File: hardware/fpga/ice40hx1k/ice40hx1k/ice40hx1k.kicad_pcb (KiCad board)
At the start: 2 copper layers, 96.8 x 77 mm, 58 parts, among them J1 Conn_01x20_Male, J2 Conn_01x20_Male, J3 Conn_01x20_Male, U1 LTC3406ES5, U5 AT25SF081-SSHD-X, U6 ICE40HX1K-VQ100(VQFP100), U7 AS7C34096A, X2 ASE-10MHz, X3 ASE-10MHz, X4 ASE-10MHz, X5 ASV-xxxMHz, X6 ASV-xxxMHz, X7 ASV-xxxMHz

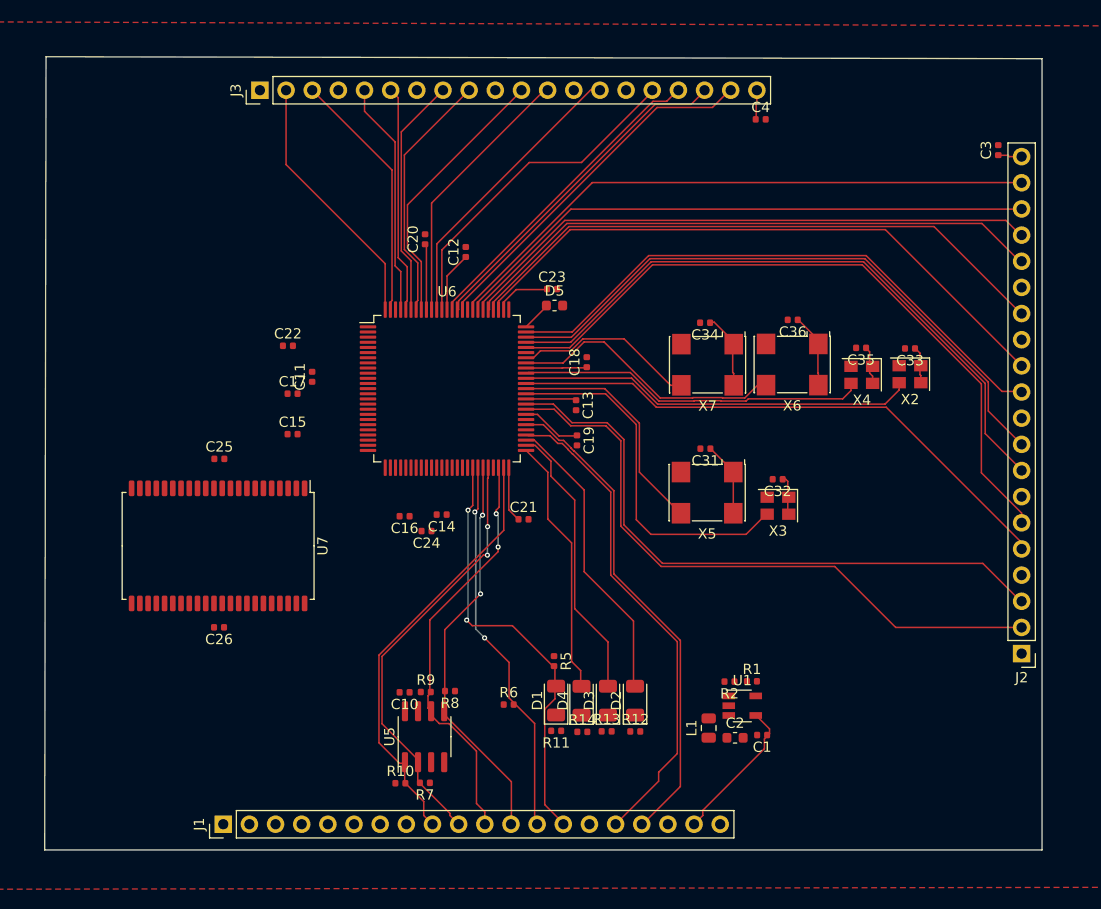
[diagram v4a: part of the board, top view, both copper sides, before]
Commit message: std FPGA skeleton
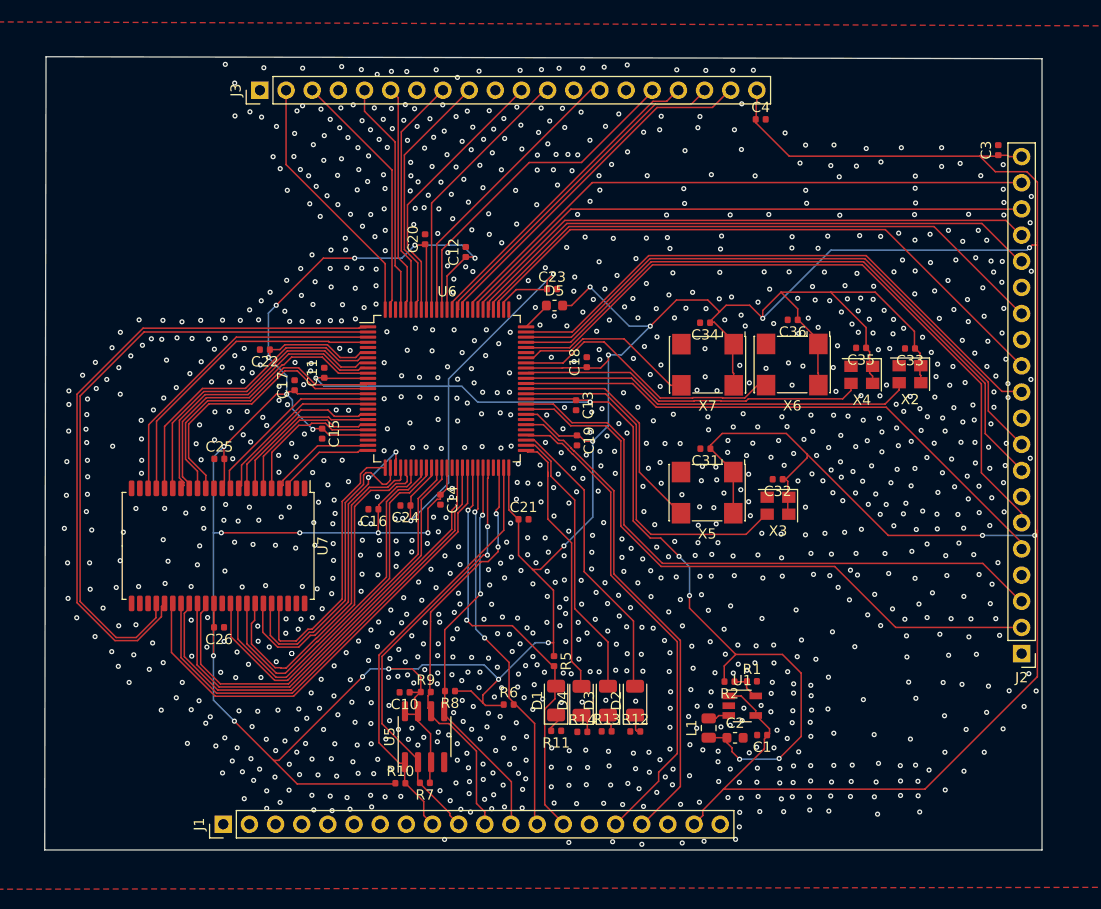
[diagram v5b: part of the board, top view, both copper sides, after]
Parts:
- moved C24 3.22 mm to (148.2, 117.5)
- moved C16 3.11 mm to (145.1, 117.8)
- moved C15 2.87 mm to (140.1, 110.5), turned to 270 degrees
- moved C22 2.27 mm to (134.5, 102.3), turned to 180 degrees
- moved C14 1.45 mm to (151.6, 116.9), turned to 270 degrees
- moved C11 1.24 mm to (140.3, 104.6)
- moved C17 0.84 mm to (137.4, 105.8), turned to 90 degrees
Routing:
- net +3V3: track 81.1 -> 593.3 mm, vias 0 -> 27
- net +1V2: track 10.4 -> 141.8 mm, vias 0 -> 8
- net IO1: track 0.00 -> 63.1 mm
- net IO2: track 0.00 -> 61.5 mm
- net IO43: track 0.00 -> 47.5 mm
- net IO41: track 0.00 -> 46.2 mm
- net IO40: track 0.00 -> 45.4 mm
- net IO37: track 0.00 -> 43.3 mm
- net IO36: track 0.00 -> 42.1 mm
- net IO34: track 0.00 -> 37.0 mm
- net IO33: track 0.00 -> 35.8 mm
- net IO30: track 0.00 -> 35.6 mm
- net IO29: track 0.00 -> 33.7 mm
- net IO28: track 0.00 -> 31.7 mm, vias 0 -> 2
- net IO3: track 0.00 -> 31.2 mm
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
